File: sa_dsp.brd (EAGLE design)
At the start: 2 parts, among them U1 10CL016YF484C6G, U2 OSD3358-512M-BSM

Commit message: Work on the DSP
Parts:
- removed U2: OSD3358-512M-BSM, Octavo-Systems:OSD335X-BGA-256
- added C10, C13, C14, C17, C2, C25, C26, C28, C3, C30, C35, C36, C37, C38, C43, C44, C47, C49, C5, C58, C59, C6, C60, C61, C62, C63, C64, C65, C66, C69, C71, C79, C8, C80, C81, C82, C83, C84, C9: 100nF 16V, CAPACITORS:0603
- added C11, C12, C16, C22, C45, C46, C48, C54, C67, C68, C7, C70, C76: 10uF 10V, CAPACITORS:0603
- added C15, C27: 15pF 50V, CAPACITORS:0603
- added C18, C19, C20, C21, C50, C51, C52, C53, C72, C73, C74, C75: 470pF 16V, CAPACITORS:0603
- added C23, C24, C56, C57, C77, C78: 330nF 16V, CAPACITORS:1206
- added CN1: uSD, CONNECTORs:114-00841-68
- added D1, D2, D3, D4: RED STATUS, OPTO:VLMT3100
- added FB10, FB11, FB12, FB13, FB14, FB15, FB16, FB2, FB5, FB7, FB8, FB9: 600R, INDUCTORS:0603
- added Q3, Q4: 2N7002, TRANSISTORs:SOT23-3
- added R10, R11, R27, R28, R38, R39: 180k, r_0603:0603
- added R108, R109, R110, R111, R112, R113, R114, R115, R18, R19, R45, R46, R47, R48, R49, R50, R51, R52, R6, R78, R79, R80, R82, R83, R92, R93, R94, R95, R96, R97, R98, R99: 470R, r_0603:0603
- added R16, R17, R20, R21, R29, R30, R31, R32, R40, R41, R42, R43, R75, R76, R77, R81: 1.0k, r_0603:0603
- added R2, R23, R24, R25, R26, R34, R35, R36, R37, R7, R8, R9: 20k, r_0603:0603
- added R22, R33, R44: 22R, RESISTORS:1206_ARRAY
- added R53: 10k, r_0603:0603
- added R54, R55, R56, R57, R58, R59, R60, R61, R62, R63, R64, R65, R66, R67, R68, R69: 100k, r_0603:0603
- added R70, R71: 10k, RESISTORS:1206_ARRAY
- added R72, R73, R74: 1.0M, r_0603:0603
- added U10, U12, U13, U15, U17, U18, U20, U4, U5: LME49720, ICs:SO8
- added U11, U16: PGA2311, ICs:SOL16
- added U14, U19, U9: PCM1754, ICs:SSOP16-4MM
- added U21, U25, U29, U7: 7 SEG, OPTO:SC56-11SURKWA
- added U22, U26, U30, U8: 74HC164A, ICs:SSOP14-4.5MM
- added U3: OSD3358-512M-BSM, Octavo-Systems:OSD335X-BGA-256
- added XTAL2: 24MHz, CRYSTALS:5X3.2SMD
- U1: value 10CL016YF484C6G -> PGA2311; device ICs:FBGA484 -> ICs:SOL16
- moved U1 128.5 mm to (120.0, 94.9)
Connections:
- removed net SYS_RTC_1P8V: U2.K11, U2.L11
- removed net SYS_VDD1_3P3V: U2.F6, U2.F7, U2.G6, U2.G7
- removed net SYS_VDD2_3P3V: U2.F11, U2.G11
- removed net SYS_VDD3_3P3V: U2.F8, U2.G8, U2.H7, U2.H8, U2.J7, U2.J8, U2.K8, U2.L8
- removed net SYS_VDD_1P8V: U2.F10, U2.G10, U2.H10, U2.H11, U2.J10, U2.J11, U2.K10, U2.L10
- removed net SYS_VOUT: U2.K6, U2.K7, U2.L6, U2.L7
- removed net VDDSHV1: U2.J9
- removed net VDDSHV2: U2.K9
- removed net VDDSHV3: U2.L9
- removed net VDDSHV4: U2.F9
- removed net VDDSHV5: U2.G9
- removed net VDDSHV6: U2.H9
- removed net VIN_AC: U2.P10, U2.R10, U2.T10
- removed net VIN_BAT: U2.P8, U2.R8, U2.T8
- removed net VIN_USB: U2.P9, U2.R9, U2.T9
- new net +5V: C25.2, C28.2, C36.2, C58.2, C60.2, C62.2, C79.2, C81.2, C83.2, FB10.1, FB12.2, FB14.1, FB16.2, FB5.1, FB8.2, U10.8, U12.8, U13.8, U15.8, U17.8, U18.8, U20.8, U4.8, U5.8
- new net -5V: C26.1, C35.1, C37.1, C59.1, C61.1, C63.1, C80.1, C82.1, C84.1, FB13.1, FB2.1, FB9.1, U10.4, U12.4, U13.4, U15.4, U17.4, U18.4, U20.4, U4.4, U5.4
- new net 3V3: C2.2, C3.2, C30.2, C5.2, C6.2, C7.2, CN1.4, R54.2, R55.2, R56.2, R70.5, R70.6, R70.7, R70.8, R71.6, R71.7, R71.8, R72.2, U22.14, U22.9, U26.14, U26.9, U30.14, U30.9, U8.14, U8.9
- new net 5V: FB11.2, FB15.2, FB7.2, U1.1, U11.1, U16.1, U3.M15, U3.P10, U3.R10, U3.T10
- new net 5VUSB: U3.J16
- new net AGND: C11.1, C12.1, C13.1, C16.1, C17.1, C18.2, C20.2, C22.1, C25.1, C26.2, C28.1, C35.2, C36.1, C37.2, C38.1, C43.1, C45.1, C46.1, C47.1, C48.1, C49.1, C50.2, C52.2, C54.1, C58.1, C59.2, C60.1, C61.2, C62.1, C63.2, C64.1, C65.1, C67.1, C68.1, C69.1, C70.1, C71.1, C72.2, C74.2, C76.1, C79.1, C8.1, C80.2, C81.1, C82.2, C83.1, C84.2, C9.1, R10.1, R11.1, R27.1, R28.1, R38.1, R39.1, U1.10, U1.15, U11.10, U11.15, U12.5, U13.5, U14.9, U16.10, U16.15, U17.5, U18.5, U19.9, U4.5, U5.5, U9.9
- new net AM_DEBUG_UART_RX: U3.A12
- new net AM_DEBUG_UART_TX: U3.B12
- new net AM_EEPROM_WP: U3.M2, U3.N3
- new net AM_PMIC_PGOOD: Q4.1, R73.2, U3.N12, U3.P11
- new net AM_PWR_BTN: U3.T11
- new net AM_STM_NRST: U3.P5
- new net AM_USR_LED0: R75.1, U3.P13
- new net AM_USR_LED1: R76.1, U3.T14
- new net AM_USR_LED2: R77.1, U3.R14
- new net AM_USR_LED3: R81.1, U3.P14
- new net AM_WARM_!RST: Q3.2, U3.R11
- new net DAC0_I2S_BCLK: R22.8, R33.8, R44.8
- new net DAC0_I2S_DATA: R22.7, R33.7, R44.7
- new net DAC0_I2S_LRCLK: R22.6, R33.6, R44.6
- new net DAC0_I2S_SCLK: R22.5, R33.5, R44.5
- new net DAC_MUTE: U14.14, U19.14, U9.14
- new net DISP_SPI_!CE: U22.2, U26.2, U30.2, U8.2
- new net DISP_SPI_MOSI: U22.1, U26.1, U30.1, U8.1
- new net DISP_SPI_SCLK: U22.8, U26.8, U30.8, U8.8
- new net GND: C10.1, C2.1, C3.1, C30.1, C44.1, C5.1, C6.1, C66.1, C7.1, CN1.6, CN1.CD_2, CN1.MNT1, CN1.MNT2, CN1.MNT3, CN1.MNT4, D1.K, D2.K, D3.K, D4.K, Q3.3, Q4.3, R53.1, R57.1, R58.1, R59.1, R60.1, R61.1, R62.1, R63.1, R64.1, R65.1, R66.1, R67.1, R68.1, R69.1, R73.1, U1.5, U11.5, U14.12, U14.13, U14.15, U14.4, U16.5, U19.12, U19.13, U19.15, U19.4, U21.3, U21.8, U22.7, U25.3, U25.8, U26.7, U29.3, U29.8, U3.D8, U3.D9, U3.E10, U3.E11, U3.E12, U3.E5, U3.E6, U3.E7, U3.E8, U3.E9, U3.F12, U3.F5, U3.G12, U3.G5, U3.H12, U3.H13, U3.H4, U3.H5, U3.J12, U3.J13, U3.J4, U3.J5, U3.K12, U3.K5, U3.L12, U3.L14, U3.L5, U3.M10, U3.M11, U3.M12, U3.M5, U3.M6, U3.M7, U3.M8, U3.M9, U3.N8, U3.N9, U30.7, U7.3, U7.8, U8.7, U9.12, U9.13, U9.15, U9.4
- new net MMC0_CD: CN1.CS_1, R71.3, U3.C14
- new net MMC0_CLK: CN1.5, R70.3, U3.B15
- new net MMC0_CMD: CN1.3, R70.4, U3.B16
- new net MMC0_D0: CN1.7, R70.2, U3.A16
- new net MMC0_D1: CN1.8, R70.1, U3.A15
- new net MMC0_D2: CN1.1, R71.2, U3.C16
- new net MMC0_D3: CN1.2, R71.1, U3.C15
- new net N$100: R41.2, U17.7
- new net N$101: C78.2, R36.1, R39.2
- new net N$102: C77.2, R34.1, R38.2
- new net N$103: R44.1, U19.1
- new net N$104: R44.2, U19.2
- new net N$105: R44.4, U19.16
- new net N$106: R44.3, U19.3
- new net N$107: C77.1, U19.8
- new net N$108: R40.1, U16.14, U17.3
- new net N$109: R19.1, U8.12
- new net N$11: C10.2, FB7.1, U1.4
- new net N$110: R6.1, U8.11
- new net N$111: R18.1, U8.10
- new net N$112: R50.2, U21.7
- new net N$113: R51.2, U21.6
- new net N$114: R52.2, U21.4
- new net N$115: R78.2, U21.2
- new net N$116: R79.1, U21.5
- new net N$117: R80.1, U21.10
- new net N$118: R82.1, U21.9
- new net N$119: R83.1, U21.1
- new net N$12: U4.1, U4.2
- new net N$120: R80.2, U22.6
- new net N$121: R82.2, U22.5
- new net N$122: R83.2, U22.3
- new net N$123: R78.1, U22.4
- new net N$124: U3.K6, U3.K7, U3.L6, U3.L7
- new net N$125: U3.F6, U3.F7, U3.G6, U3.G7
- new net N$126: U3.F11, U3.G11
- new net N$127: U3.K11, U3.L11
- new net N$128: U3.F8, U3.F9, U3.G8, U3.G9, U3.H7, U3.H8, U3.H9, U3.J7, U3.J8, U3.J9, U3.K8, U3.K9, U3.L8, U3.L9
- new net N$129: U3.F10, U3.G10, U3.H10, U3.H11, U3.J10, U3.J11, U3.K10, U3.L10
- new net N$13: R16.2, R17.1, U4.6
- new net N$130: U3.N10, U3.N11
- new net N$131: U3.N4, U3.N5
- new net N$132: U3.L4, U3.M4
- new net N$133: U3.D4, U3.E4
- new net N$134: U3.C10, U3.D10
- new net N$135: U3.C11, U3.D11
- new net N$136: R53.2, U3.M16
- new net N$137: R57.2, U3.G3
- new net N$138: R58.2, U3.G2
- new net N$139: R59.2, U3.G1
- new net N$140: R54.1, U3.H3
- new net N$141: R55.1, U3.H2
- new net N$142: R60.2, U3.H1
- new net N$143: R61.2, U3.J3
- new net N$144: R62.2, U3.J2
- new net N$145: R63.2, U3.J1
- new net N$146: R64.2, U3.K3
- new net N$147: R65.2, U3.K2
- new net N$148: R66.2, U3.K1
- new net N$149: R67.2, U3.L3
- new net N$150: R68.2, U3.L2
- new net N$151: R56.1, U3.L1
- new net N$152: R69.2, U3.M3
- new net N$153: U3.P9, U3.R9, U3.T9
- new net N$154: U3.N7, U3.P8, U3.R8, U3.T8
- new net N$155: C14.2, U3.A7, U3.B7
- new net N$156: C14.1, U3.A9, U3.B9
- new net N$157: Q3.1, Q4.2, R72.1
- new net N$158: C27.2, R74.1, U3.N16, XTAL2.2
- new net N$159: C15.2, R74.2, U3.P16, XTAL2.1
- new net N$160: C15.1, C27.1, U3.N15
- new net N$161: U3.D6, U3.D7
- new net N$162: D1.A, R75.2
- new net N$163: D2.A, R76.2
- new net N$164: D3.A, R77.2
- new net N$165: D4.A, R81.2
- new net N$166: R52.1, U22.12
- new net N$167: R50.1, U22.11
- new net N$168: R51.1, U22.10
- new net N$17: U5.1, U5.2
- new net N$184: R92.2, U25.7
- new net N$185: R93.2, U25.6
- new net N$186: R94.2, U25.4
- new net N$187: R95.2, U25.2
- new net N$188: R96.1, U25.5
- new net N$189: R97.1, U25.10
- new net N$190: R98.1, U25.9
- new net N$191: R99.1, U25.1
- new net N$192: R97.2, U26.6
- new net N$193: R98.2, U26.5
- new net N$194: R99.2, U26.3
- new net N$195: R95.1, U26.4
- new net N$196: R94.1, U26.12
- new net N$197: R92.1, U26.11
- new net N$198: R93.1, U26.10
- new net N$214: R108.2, U29.7
- new net N$215: R109.2, U29.6
- new net N$216: R110.2, U29.4
- new net N$217: R111.2, U29.2
- new net N$218: R112.1, U29.5
- new net N$219: R113.1, U29.10
- new net N$22: R6.2, U7.7
- new net N$220: R114.1, U29.9
- new net N$221: R115.1, U29.1
- new net N$222: R113.2, U30.6
- new net N$223: R114.2, U30.5
- new net N$224: R115.2, U30.3
- new net N$225: R111.1, U30.4
- new net N$226: R110.1, U30.12
- new net N$227: R108.1, U30.11
- new net N$228: R109.1, U30.10
- new net N$23: R18.2, U7.6
- new net N$24: R19.2, U7.4
- new net N$25: R45.2, U7.2
- new net N$26: R20.1, U1.11, U5.3
- new net N$27: R20.2, R21.1, U5.6
- new net N$28: R21.2, U5.7
- new net N$29: C13.2, C22.2, FB8.1, U9.6
- new net N$30: R46.1, U7.5
- new net N$31: R47.1, U7.10
- new net N$32: R48.1, U7.9
- new net N$33: R49.1, U7.1
- new net N$34: C16.2, C17.2, U9.10
- new net N$35: R47.2, U8.6
- new net N$36: C19.2, R2.2, R7.1
- new net N$37: C18.1, R7.2, U10.3
- new net N$38: R48.2, U8.5
- new net N$39: R49.2, U8.3
- new net N$40: C19.1, U1.9, U10.1, U10.2
- new net N$41: C21.2, R8.2, R9.1
- new net N$42: C20.1, R9.2, U10.5
- new net N$43: R45.1, U8.4
- new net N$44: C21.1, U1.16, U10.6, U10.7
- new net N$45: C24.1, U9.7
- new net N$46: R17.2, U4.7
- new net N$47: C24.2, R11.2, R8.1
- new net N$48: C23.2, R10.2, R2.1
- new net N$49: R22.1, U9.1
- new net N$50: R22.2, U9.2
- new net N$51: R22.4, U9.16
- new net N$52: R22.3, U9.3
- new net N$53: C23.1, U9.8
- new net N$54: R16.1, U1.14, U4.3
- new net N$55: C38.2, C45.2, FB9.2, U11.13
- new net N$56: C43.2, C46.2, FB10.2, U11.12
- new net N$57: C44.2, FB11.1, U11.4
- new net N$58: U12.1, U12.2
- new net N$59: R29.2, R30.1, U12.6
- new net N$60: U13.1, U13.2
- new net N$61: R31.1, U11.11, U13.3
- new net N$62: R31.2, R32.1, U13.6
- new net N$63: R32.2, U13.7
- new net N$64: C47.2, C54.2, FB12.1, U14.6
- new net N$65: C48.2, C49.2, U14.10
- new net N$66: C51.2, R23.2, R24.1
- new net N$67: C50.1, R24.2, U15.3
- new net N$68: C51.1, U11.9, U15.1, U15.2
- new net N$69: C53.2, R25.2, R26.1
- new net N$70: C52.1, R26.2, U15.5
- new net N$71: C53.1, U11.16, U15.6, U15.7
- new net N$72: C57.1, U14.7
- new net N$73: R30.2, U12.7
- new net N$74: C57.2, R25.1, R28.2
- new net N$75: C56.2, R23.1, R27.2
- new net N$76: R33.1, U14.1
- new net N$77: R33.2, U14.2
- new net N$78: R33.4, U14.16
- new net N$79: R33.3, U14.3
- new net N$8: C11.2, C8.2, FB2.2, U1.13
- new net N$80: C56.1, U14.8
- new net N$81: R29.1, U11.14, U12.3
- new net N$82: C64.2, C67.2, FB13.2, U16.13
- new net N$83: C65.2, C68.2, FB14.2, U16.12
- new net N$84: C66.2, FB15.1, U16.4
- new net N$85: U17.1, U17.2
- new net N$86: R40.2, R41.1, U17.6
- new net N$87: U18.1, U18.2
- new net N$88: R42.1, U16.11, U18.3
- new net N$89: R42.2, R43.1, U18.6
- new net N$9: C12.2, C9.2, FB5.2, U1.12
- new net N$90: R43.2, U18.7
- new net N$91: C69.2, C76.2, FB16.1, U19.6
- new net N$92: C70.2, C71.2, U19.10
- new net N$93: C73.2, R34.2, R35.1
- new net N$94: C72.1, R35.2, U20.3
- new net N$95: C73.1, U16.9, U20.1, U20.2
- new net N$96: C75.2, R36.2, R37.1
- new net N$97: C74.1, R37.2, U20.5
- new net N$98: C75.1, U16.16, U20.6, U20.7
- new net N$99: C78.1, U19.7
- new net PGA0_!CS: U1.2, U11.2, U16.2
- new net PGA_!MUTE: U1.8, U11.8, U16.8
- new net PGA_SCLK: U1.6, U11.6, U16.6
- new net PGA_SDI: U1.3, U11.3, U16.3
- new net SHIFT_OUT: R112.2, R46.2, R79.2, R96.2, U22.13, U26.13, U30.13, U8.13
- new net STM32_BOOT0: U3.R5
- new net STM_AM_UART_RX: U3.B11
- new net STM_AM_UART_TX: U3.A11
- new net USB0_DM: U3.K16
- new net USB0_DP: U3.K15
- new net USB0_ID: U3.K14
- new net USB1_DM: U3.L16
- new net USB1_DP: U3.L15
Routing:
- net AGND: track 0.00 -> 114.4 mm, vias 0 -> 90
- net GND: track 0.00 -> 91.4 mm, vias 0 -> 77
- net PGA_!MUTE: track 0.00 -> 34.9 mm
- net PGA_SCLK: track 0.00 -> 32.3 mm
- net PGA0_!CS: track 0.00 -> 32.3 mm
- net DAC_MUTE: track 0.00 -> 32.3 mm
- net +5V: track 0.00 -> 31.7 mm, vias 0 -> 15
- net PGA_SDI: track 0.00 -> 31.2 mm
- net N$98: track 0.00 -> 30.0 mm
- net N$71: track 0.00 -> 30.0 mm
- net N$44: track 0.00 -> 30.0 mm
- net -5V: track 0.00 -> 28.3 mm, vias 0 -> 12
- net 3V3: track 0.00 -> 28.0 mm, vias 0 -> 14
- net N$128: track 0.00 -> 24.1 mm
- net N$81: track 0.00 -> 23.9 mm
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- added copper zone on layer 3, net 3V3
- added copper zone on layer 2, net GND
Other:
- board outline added: 150 x 110 mm

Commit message: Added FPGA
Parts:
- added C100, C101, C102, C103, C104, C105, C106, C107, C109, C110, C111, C112, C113, C114, C115, C116, C117, C118, C96, C97, C98, C99: 100nF 16V, CAPACITORS:0402
- added C108: 4.7uF 16V, CAPACITORS:0402
- added CN3: 2X5 HEADER, CONNECTORs:5X2_2.54MMHEADER
- added MECH1, MECH2, MECH3, MECH4: 6mm x 3mm, MISC:MOUNTHOLE_6X3
- added R14: 1.0k, r_0603:0603
- added R15, R84, R85, R86, R87: 10k, r_0603:0603
- added U6: 10CL016YF484C6G, ICs:FBGA484
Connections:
- new net 1V2: C100.2, C101.2, C102.2, C103.2, C104.2, C105.2, C106.2, C107.2, C108.2, U6.E17, U6.F6, U6.J10, U6.J11, U6.J12, U6.J13, U6.J14, U6.J8, U6.K14, U6.K9, U6.L14, U6.L9, U6.M14, U6.M9, U6.N9, U6.P10, U6.P11, U6.P12, U6.P13, U6.P9, U6.T13, U6.U16, U6.U17, U6.U6, U6.V17
- new net 2V5: C96.2, C97.2, C98.2, C99.2, U6.F18, U6.G6, U6.T6, U6.U18
- new net CONF_CONFDN: R86.1, U6.M18
- new net CONF_JTAG_TCK: CN3.1, R14.2, U6.L2
- new net CONF_JTAG_TDI: CN3.5, R84.1, U6.L5
- new net CONF_JTAG_TDO: CN3.2, U6.L4
- new net CONF_JTAG_TMS: CN3.3, R15.1, U6.L1
- new net CONF_NCONFIG: R87.1
- new net CONF_NSTATUS: R85.1, U6.K6
- net 3V3: now also C109.2, C110.2, C111.2, C112.2, C113.2, C114.2, C115.2, C116.2, C117.2, C118.2, CN3.9, R15.2, R84.2, R85.2, R86.2, R87.2, U6.A2, U6.A21, U6.AA6, U6.AB2, U6.AB21, U6.D11, U6.D12, U6.D14, U6.D16, U6.D18, U6.D4, U6.D5, U6.D9, U6.E19, U6.E8, U6.F4, U6.G19, U6.H4, U6.J20, U6.K4, U6.K5, U6.L19, U6.N4, U6.P18, U6.R4, U6.T19, U6.U4, U6.V19, U6.W11, U6.W12, U6.W16, U6.W18, U6.W4, U6.W5, U6.W9, U6.Y14, U6.Y19
- net GND: now also C100.1, C101.1, C102.1, C103.1, C104.1, C105.1, C106.1, C107.1, C108.1, C109.1, C110.1, C111.1, C112.1, C113.1, C114.1, C115.1, C116.1, C117.1, C118.1, C96.1, C97.1, C98.1, C99.1, CN3.10, CN3.6, R14.1, U6.A1, U6.A22, U6.AA1, U6.AA17, U6.AA2, U6.AB1, U6.AB17, U6.AB22, U6.AB6, U6.C1, U6.C11, U6.C12, U6.C14, U6.C16, U6.C18, U6.C2, U6.C5, U6.C9, U6.D3, U6.D7, U6.D8, U6.E18, U6.E20, U6.F3, U6.F5, U6.G20, U6.H3, U6.H8, U6.J19, U6.J5, U6.J9, U6.K1, U6.K10, U6.K11, U6.K12, U6.K13, U6.K2, U6.K20, U6.K3, U6.L10, U6.L11, U6.L12, U6.L13, U6.L17, U6.L18, U6.L20, U6.L3, U6.M10, U6.M11, U6.M12, U6.M13, U6.M17, U6.N10, U6.N11, U6.N12, U6.N13, U6.N3, U6.P19, U6.R3, U6.T20, U6.U3, U6.U5, U6.V18, U6.V20, U6.W3, U6.Y11, U6.Y12, U6.Y15, U6.Y16, U6.Y18, U6.Y20, U6.Y5, U6.Y9
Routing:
- net GND: track 91.4 -> 175.1 mm, vias 77 -> 143
- net 3V3: track 28.0 -> 65.8 mm, vias 14 -> 48
- net 1V2: track 0.00 -> 32.0 mm, vias 0 -> 27
- net 2V5: track 0.00 -> 6.83 mm, vias 0 -> 4
- added copper zone on layer 3, net 1V2
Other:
- outline, holes or cut-outs redrawn

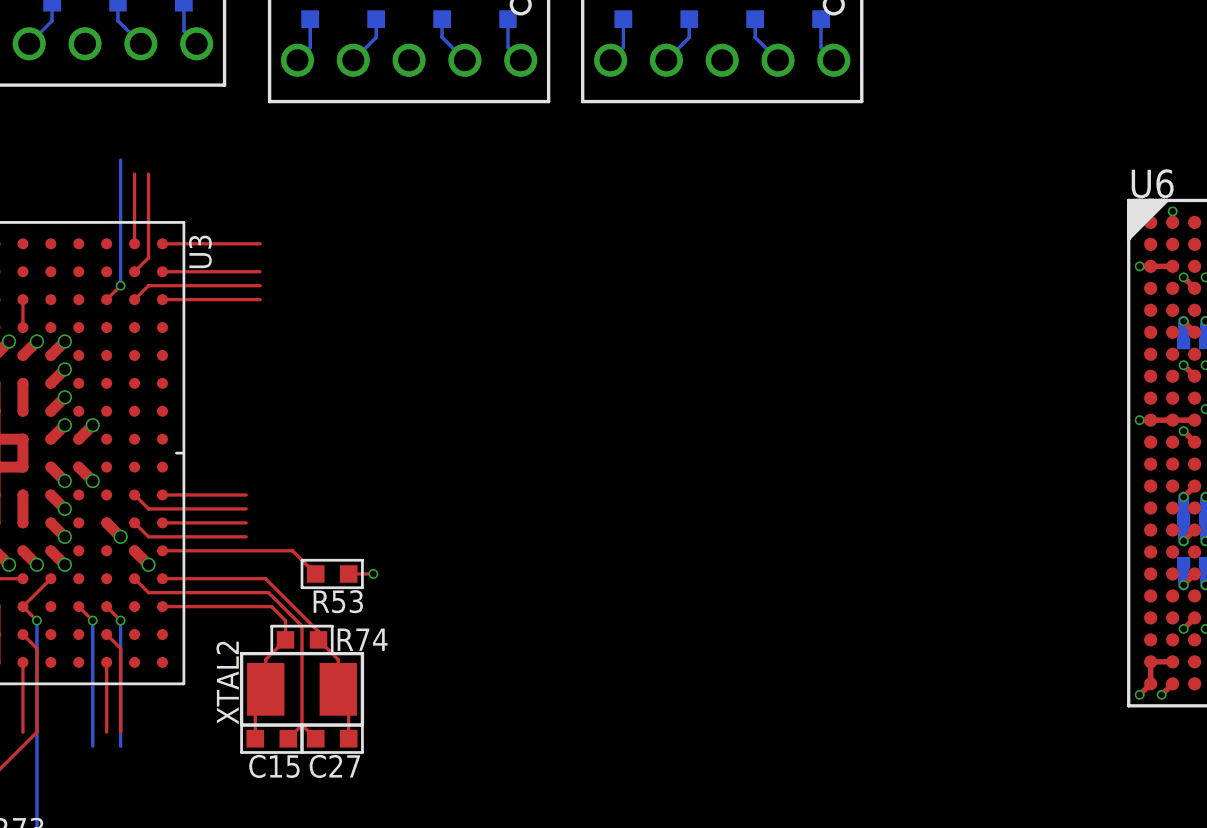
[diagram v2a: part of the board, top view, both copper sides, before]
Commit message: USB added
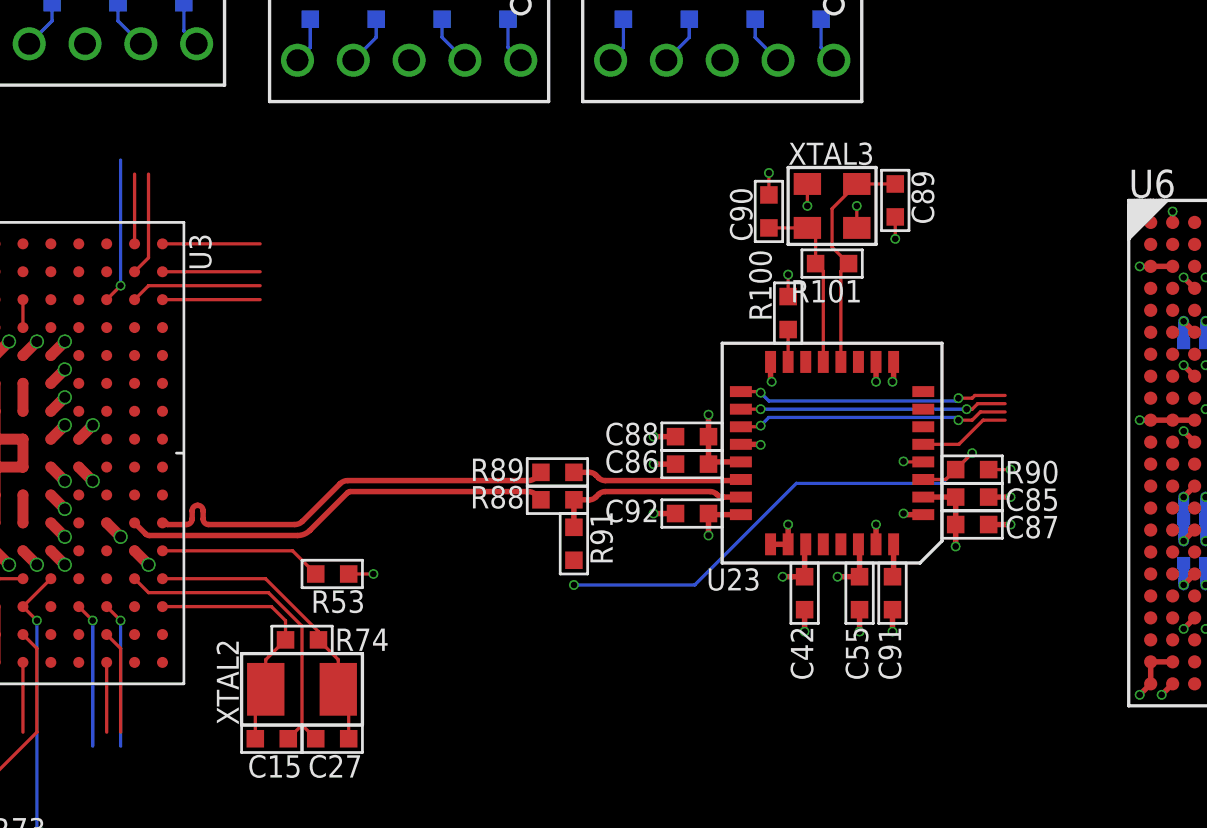
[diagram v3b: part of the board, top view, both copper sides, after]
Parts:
- added C42, C55, C85, C86, C92: 100nF 16V, CAPACITORS:0603
- added C87, C88, C91: 10uF 10V, CAPACITORS:0603
- added C89, C90: 10pF 100V, CAPACITORS:0603
- added R100, R91: 1.5k, r_0603:0603
- added R101: 1.0M, r_0603:0603
- added R88, R89: 22R, r_0603:0603
- added R90: 10k, r_0603:0603
- added U23: PCM2707, ICs:QFP32_0.8MM
- added XTAL3: 12MHz, CRYSTALS:3.2X3.5SMD
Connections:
- removed net 5VUSB: U3.J16
- removed net USB0_DM: U3.K16
- removed net USB0_DP: U3.K15
- removed net USB0_ID: U3.K14
- removed net USB1_DM: U3.L16
- removed net USB1_DP: U3.L15
- new net N$14: C89.2, R101.1, U23.12, XTAL3.3
- new net N$15: C90.2, R101.2, U23.13, XTAL3.1
- new net N$16: R88.2, R91.1, U23.23
- new net N$169: R100.1, U23.15
- new net N$18: R89.2, U23.22
- new net N$21: C91.2, U23.32
- new net OSD_USB1_DM: R89.1, U3.L16
- new net OSD_USB1_DP: R88.1, U3.L15
- new net PCM_I2S_BCLK: U23.19
- new net PCM_I2S_DOUT: U23.17
- new net PCM_I2S_LRCLK: U23.5
- new net PCM_I2S_MCLK: U23.18
- net 3V3: now also C42.2, C55.2, C85.2, C86.2, C87.2, C88.2, C92.2, R100.2, U23.10, U23.2, U23.21, U23.24, U23.27, U23.30
- net 5V: now also R90.2, R91.2, U23.3
- net GND: now also C42.1, C55.1, C85.1, C86.1, C87.1, C88.1, C89.1, C90.1, C91.1, C92.1, R90.1, U23.1, U23.16, U23.20, U23.25, U23.26, U23.31, U23.4, U23.9, XTAL3.2, XTAL3.4
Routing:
- net 5V: track 11.3 -> 34.6 mm, vias 7 -> 9
- net GND: track 175.1 -> 195.3 mm, vias 143 -> 163
- net OSD_USB1_DP: track 0.00 -> 19.6 mm
- net OSD_USB1_DM: track 0.00 -> 19.3 mm
- net 3V3: track 65.8 -> 82.7 mm, vias 48 -> 55
- net PCM_I2S_BCLK: track 0.00 -> 12.4 mm, vias 0 -> 2
- net PCM_I2S_DOUT: track 0.00 -> 12.3 mm, vias 0 -> 2
- net PCM_I2S_MCLK: track 0.00 -> 12.1 mm, vias 0 -> 2
- net N$14: track 0.00 -> 10.8 mm
- net N$16: track 0.00 -> 9.00 mm
- net N$15: track 0.00 -> 8.15 mm
- net N$18: track 0.00 -> 7.71 mm
- net USB1_DP: track 5.34 -> 0.00 mm
- net USB0_DP: track 5.34 -> 0.00 mm
- net PCM_I2S_LRCLK: track 0.00 -> 4.18 mm
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
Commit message: Additions
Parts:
- added C1, C119, C125, C29, C4, C93, C94, C95: 100nF 16V, CAPACITORS:0603
- added C120, C121, C124: 10uF 10V, CAPACITORS:0603
- added C122, C123: 10pF 100V, CAPACITORS:0603
- added R1, R104, R12, R3: 10k, r_0603:0603
- added R102, R103: 22R, r_0603:0603
- added R105, R106: 1.5k, r_0603:0603
- added R107: 1.0M, r_0603:0603
- added R13, R4, R5: 1.0k, r_0603:0603
- added RE1: PEC11, ELECTROMECH:PEC11R-4XXXF-SXXXX
- added U24: PCM2707, ICs:QFP32_0.8MM
- added XTAL4: 12MHz, CRYSTALS:3.2X3.5SMD
- moved R71 44.7 mm to (48.0, 61.0), turned to 270 degrees
- moved CN1 39.8 mm to (48.0, 63.5), turned to 270 degrees
- moved C6 39.5 mm to (51.2, 64.6), turned to 270 degrees
- moved C7 38.7 mm to (50.0, 64.6), turned to 270 degrees
- moved R15 37.1 mm to (93.0, 12.5)
- moved R84 37.1 mm to (96.5, 12.5)
- moved R85 37.1 mm to (100.0, 12.5)
- moved R86 37.1 mm to (93.0, 9.25)
- moved R87 37.1 mm to (96.5, 9.25)
- moved R70 34.9 mm to (48.0, 66.0), turned to 270 degrees
- moved CN3 22.6 mm to (98.8, 5.75), turned to 90 degrees
- moved R14 18.3 mm to (100.0, 9.00)
- moved C30 8.51 mm to (56.8, 78.1)
- moved R108 8.51 mm to (53.0, 85.0)
- moved R109 8.51 mm to (56.0, 85.0)
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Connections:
- net PCM_I2S_BCLK renamed PCM_I2S_BCLK_BB
- net PCM_I2S_DOUT renamed PCM_I2S_DOUT_BB
- net PCM_I2S_LRCLK renamed PCM_I2S_LRCLK_BB
- net PCM_I2S_MCLK renamed PCM_I2S_MCLK_BB
- new net 5VUSB: R104.2, R105.2, U24.3
- new net ENC_A: C1.2, R4.2
- new net ENC_B: C4.2, R5.2
- new net ENC_SW: C29.2, R13.1
- new net N$1: R1.1, R4.1, RE1.A
- new net N$170: R102.2, R105.1, U24.23
- new net N$171: R103.2, U24.22
- new net N$172: R102.1
- new net N$173: R103.1
- new net N$174: C124.2, U24.32
- new net N$175: R106.1, U24.15
- new net N$19: C122.2, R107.1, U24.12, XTAL4.3
- new net N$2: R3.1, R5.1, RE1.B
- new net N$20: C123.2, R107.2, U24.13, XTAL4.1
- new net N$5: R12.1, R13.2, RE1.S
- new net PCM_I2S_BCLK_EXT: U24.19
- new net PCM_I2S_DOUT_EXT: U24.17
- new net PCM_I2S_LRCLK_EXT: U24.5
- new net PCM_I2S_MCLK_EXT: U24.18
- net 3V3: now also C119.2, C120.2, C121.2, C125.2, C93.2, C94.2, C95.2, R1.2, R106.2, R12.2, R3.2, U24.10, U24.2, U24.21, U24.24, U24.27, U24.30
- net GND: now also C1.1, C119.1, C120.1, C121.1, C122.1, C123.1, C124.1, C125.1, C29.1, C4.1, C93.1, C94.1, C95.1, R104.1, RE1.1, RE1.2, RE1.C, RE1.W, U24.1, U24.16, U24.20, U24.25, U24.26, U24.31, U24.4, U24.9, XTAL4.2, XTAL4.4
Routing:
- net GND: track 195.3 -> 215.4 mm, vias 163 -> 183
- net 3V3: track 82.7 -> 99.6 mm, vias 55 -> 62
- net N$19: track 0.00 -> 10.8 mm
- net 5VUSB: track 0.00 -> 10.5 mm, vias 0 -> 1
- net N$170: track 0.00 -> 9.00 mm
- net MMC0_CD: track 12.2 -> 21.1 mm, vias 2 -> 3
- net N$20: track 0.00 -> 8.15 mm
- net N$171: track 0.00 -> 7.71 mm
- net MMC0_D1: track 19.1 -> 23.1 mm
- net MMC0_CLK: track 20.4 -> 22.9 mm
- net N$174: track 0.00 -> 1.50 mm
- net N$175: track 0.00 -> 1.48 mm
- net MMC0_D2: track 20.3 -> 21.7 mm
- net MMC0_D3: track 21.6 -> 22.9 mm
- net MMC0_CMD: track 20.6 -> 21.9 mm
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
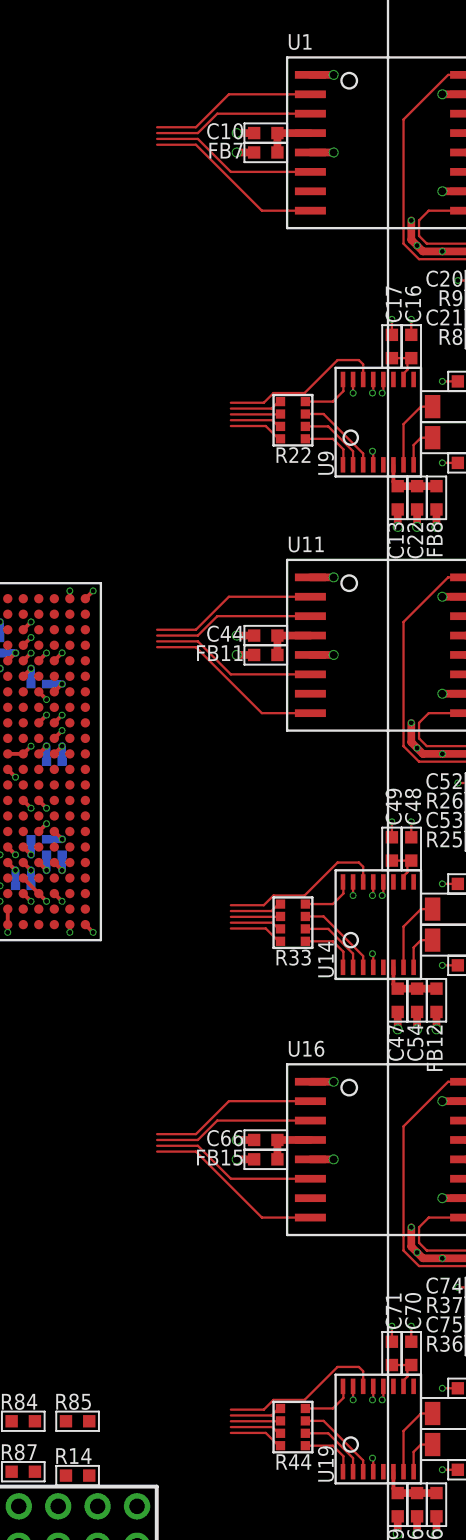
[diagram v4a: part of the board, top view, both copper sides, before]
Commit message: Routing the DACs to the FPGA
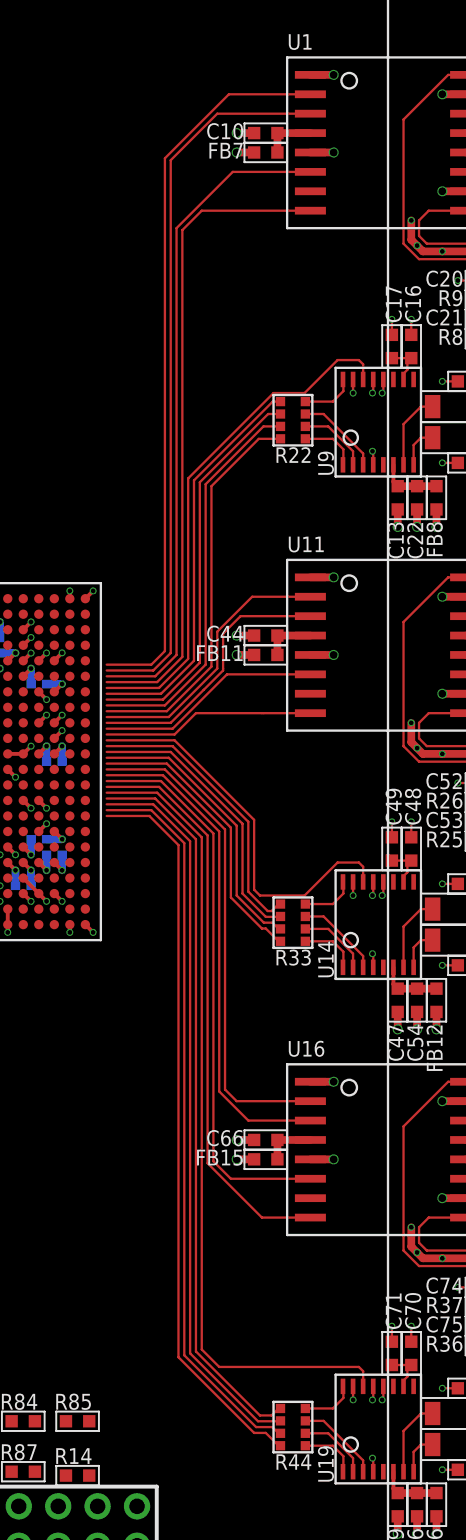
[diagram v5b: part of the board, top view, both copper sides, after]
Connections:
- removed net DAC_MUTE: U14.14, U19.14, U9.14
- removed net PGA_!MUTE: U1.8, U11.8, U16.8
- removed net PGA_SCLK: U1.6, U11.6, U16.6
- removed net PGA_SDI: U1.3, U11.3, U16.3
- new net DAC0_MUTE: U19.14
- new net DAC1_I2S_BCLK: R33.8
- new net DAC1_I2S_DATA: R33.7
- new net DAC1_I2S_LRCLK: R33.6
- new net DAC1_I2S_SCLK: R33.5
- new net DAC1_MUTE: U14.14
- new net DAC2_I2S_BCLK: R22.8
- new net DAC2_I2S_DATA: R22.7
- new net DAC2_I2S_LRCLK: R22.6
- new net DAC2_I2S_SCLK: R22.5
- new net DAC2_MUTE: U9.14
- new net PGA0_!MUTE: U16.8
- new net PGA0_SCLK: U16.6
- new net PGA0_SDI: U16.3
- new net PGA1_!CS: U11.2
- new net PGA1_!MUTE: U11.8
- new net PGA1_SCLK: U11.6
- new net PGA1_SDI: U11.3
- new net PGA2_!CS: U1.2
- new net PGA2_!MUTE: U1.8
- new net PGA2_SCLK: U1.6
- new net PGA2_SDI: U1.3
- net DAC0_I2S_BCLK: no longer R22.8, R33.8
- net DAC0_I2S_DATA: no longer R22.7, R33.7
- net DAC0_I2S_LRCLK: no longer R22.6, R33.6
- net DAC0_I2S_SCLK: no longer R22.5, R33.5
- net PGA0_!CS: no longer U1.2, U11.2
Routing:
- net DAC0_MUTE: track 0.00 -> 52.3 mm
- net PGA2_!CS: track 0.00 -> 46.9 mm
- net PGA2_SDI: track 0.00 -> 46.6 mm
- net PGA2_SCLK: track 0.00 -> 42.7 mm
- net PGA2_!MUTE: track 0.00 -> 41.8 mm
- net DAC0_I2S_LRCLK: track 9.63 -> 47.0 mm
- net DAC0_I2S_DATA: track 10.1 -> 47.2 mm
- net DAC0_I2S_SCLK: track 10.2 -> 47.2 mm
- net PGA0_!MUTE: track 0.00 -> 37.0 mm
- net DAC0_I2S_BCLK: track 10.6 -> 47.3 mm
- net PGA0_SCLK: track 0.00 -> 36.1 mm
- net PGA_!MUTE: track 34.9 -> 0.00 mm
- net DAC2_MUTE: track 0.00 -> 33.2 mm
- net PGA_SCLK: track 32.3 -> 0.00 mm
- net DAC_MUTE: track 32.3 -> 0.00 mm
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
